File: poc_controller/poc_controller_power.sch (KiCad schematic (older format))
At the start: 8 parts

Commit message: Start assigning footprints and cleaning things up.
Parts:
- removed C? (x3): CP1, symbol CP1
- removed R?: R_Shunt, symbol R_Shunt
- added C13, C14, C15: 0.1uF, Capacitors_SMD:C_1206_HandSoldering, symbol C
- added R7: 0.001, Resistors_SMD:R_1206_HandSoldering, symbol R
- J6: renamed from J?; footprint (none) -> Connectors_Terminal_Blocks:TerminalBlock_bornier-2_P5.08mm; Part Number (none) -> ED1643-ND
- R8: renamed from R?; value R -> 15k; footprint (none) -> Resistors_SMD:R_1206_HandSoldering; Part Number (none) -> 311-15KERCT-ND
- R9: renamed from R?; value R -> 3.9k; footprint (none) -> Resistors_SMD:R_1206_HandSoldering; Part Number (none) -> 311-3.9KERCT-ND
- U6: renamed from U?; footprint (none) -> TO_SOT_Packages_SMD:TSOT-23-6; Part Number (none) -> 576-2749-1-ND
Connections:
- wire segments 20 -> 22
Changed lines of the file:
@@
 $Descr A4 11693 8268
 encoding utf-8
-Sheet 3 3
+Sheet 3 4
 Title ""
 Date ""
@@
 $EndDescr
 $Comp
-L CONN_01X02 J?
+L CONN_01X02 J6
 U 1 1 5A04E548
 P 3650 2250
-F 0 "J?" H 3650 2400 50  0000 C CNN
+F 0 "J6" H 3650 2400 50  0000 C CNN
 F 1 "CONN_01X02" V 3750 2250 50  0000 C CNN
-F 2 "" H 3650 2250 50  0001 C CNN
+F 2 "Connectors_Terminal_Blocks:TerminalBlock_bornier-2_P5.08mm" H 3650 2250 50  0001 C CNN
 F 3 "" H 3650 2250 50  0001 C CNN
+F 4 "ED1643-ND" H 3650 2250 60  0001 C CNN "Part Number"
 	1    3650 2250
 	1    0    0    -1
 $EndComp
 $Comp
-L R_Shunt R?
-U 1 1 5A04E5FB
-P 3050 2200
-F 0 "R?" V 2875 2200 50  0000 C CNN
-F 1 "R_Shunt" V 2950 2200 50  0000 C CNN
-F 2 "" V 2980 2200 50  0001 C CNN
-F 3 "" H 3050 2200 50  0001 C CNN
-	1    3050 2200
-	0    -1   -1   0
-$EndComp
-$Comp
-L VDD #PWR?
+L VDD #PWR31
 U 1 1 5A04E6EA
 P 2600 2100
-F 0 "#PWR?" H 2600 1950 50  0001 C CNN
+F 0 "#PWR31" H 2600 1950 50  0001 C CNN
 F 1 "VDD" H 2600 2250 50  0000 C CNN
 F 2 "" H 2600 2100 50  0001 C CNN
@@
 $EndComp
 $Comp
-L GND #PWR?
+L GND #PWR32
 U 1 1 5A04E708
 P 3300 2500
-F 0 "#PWR?" H 3300 2250 50  0001 C CNN
+F 0 "#PWR32" H 3300 2250 50  0001 C CNN
 F 1 "GND" H 3300 2350 50  0000 C CNN
 F 2 "" H 3300 2500 50  0001 C CNN
@@
 	1    0    0    -1
 $EndComp
-Text Label 3150 2050 1    60   ~ 0
+Text Label 3300 2050 1    60   ~ 0
 BATT_CURR_POS
-Text Label 2950 2050 1    60   ~ 0
+Text Label 2850 2050 1    60   ~ 0
 BATT_CURR_NEG
 $Comp
-L VDD #PWR?
+L VDD #PWR33
 U 1 1 5A04E87F
 P 5150 1450
-F 0 "#PWR?" H 5150 1300 50  0001 C CNN
+F 0 "#PWR33" H 5150 1300 50  0001 C CNN
 F 1 "VDD" H 5150 1600 50  0000 C CNN
 F 2 "" H 5150 1450 50  0001 C CNN
@@
 $EndComp
 $Comp
-L R R?
+L R R8
 U 1 1 5A04E899
 P 5150 1750
-F 0 "R?" V 5230 1750 50  0000 C CNN
-F 1 "R" V 5150 1750 50  0000 C CNN
-F 2 "" V 5080 1750 50  0001 C CNN
+F 0 "R8" V 5230 1750 50  0000 C CNN
+F 1 "15k" V 5150 1750 50  0000 C CNN
+F 2 "Resistors_SMD:R_1206_HandSoldering" V 5080 1750 50  0001 C CNN
 F 3 "" H 5150 1750 50  0001 C CNN
+F 4 "311-15KERCT-ND" V 5150 1750 60  0001 C CNN "Part Number"
 	1    5150 1750
 	1    0    0    -1
 $EndComp
 $Comp
-L R R?
+L R R9
 U 1 1 5A04E8C1
 P 5150 2250
-F 0 "R?" V 5230 2250 50  0000 C CNN
-F 1 "R" V 5150 2250 50  0000 C CNN
-F 2 "" V 5080 2250 50  0001 C CNN
+F 0 "R9" V 5230 2250 50  0000 C CNN
+F 1 "3.9k" V 5150 2250 50  0000 C CNN
+F 2 "Resistors_SMD:R_1206_HandSoldering" V 5080 2250 50  0001 C CNN
 F 3 "" H 5150 2250 50  0001 C CNN
+F 4 "311-3.9KERCT-ND" V 5150 2250 60  0001 C CNN "Part Number"
 	1    5150 2250
 	1    0    0    -1
 $EndComp
 $Comp
-L GND #PWR?
+L GND #PWR34
 U 1 1 5A04E8E3
 P 5150 2600
-F 0 "#PWR?" H 5150 2350 50  0001 C CNN
+F 0 "#PWR34" H 5150 2350 50  0001 C CNN
 F 1 "GND" H 5150 2450 50  0000 C CNN
 F 2 "" H 5150 2600 50  0001 C CNN
@@
 BATT_VOLT
 $Comp
-L MIC5211 U?
+L MIC5211 U6
 U 1 1 5A04EB3F
 P 7100 1850
-F 0 "U?" H 7450 1850 60  0000 C CNN
+F 0 "U6" H 7450 1850 60  0000 C CNN
 F 1 "MIC5211" H 7100 1850 60  0000 C CNN
-F 2 "" H 7100 1850 60  0001 C CNN
+F 2 "TO_SOT_Packages_SMD:TSOT-23-6" H 7100 1850 60  0001 C CNN
 F 3 "" H 7100 1850 60  0001 C CNN
+F 4 "576-2749-1-ND" H 7100 1850 60  0001 C CNN "Part Number"
 	1    7100 1850
 	1    0    0    -1
 $EndComp
 $Comp
-L GND #PWR?
+L GND #PWR36
 U 1 1 5A04EB7D
 P 6450 2350
-F 0 "#PWR?" H 6450 2100 50  0001 C CNN
+F 0 "#PWR36" H 6450 2100 50  0001 C CNN
 F 1 "GND" H 6450 2200 50  0000 C CNN
 F 2 "" H 6450 2350 50  0001 C CNN
@@
 $EndComp
 $Comp
-L VDD #PWR?
+L VDD #PWR35
 U 1 1 5A04EBA0
 P 6150 1800
-F 0 "#PWR?" H 6150 1650 50  0001 C CNN
+F 0 "#PWR35" H 6150 1650 50  0001 C CNN
 F 1 "VDD" H 6150 1950 50  0000 C CNN
 F 2 "" H 6150 1800 50  0001 C CNN
@@
 $EndComp
 $Comp
-L CP1 C?
-U 1 1 5A04EC9E
-P 7800 2500
-F 0 "C?" H 7825 2600 50  0000 L CNN
-F 1 "CP1" H 7825 2400 50  0000 L CNN
-F 2 "" H 7800 2500 50  0001 C CNN
-F 3 "" H 7800 2500 50  0001 C CNN
-	1    7800 2500
-	1    0    0    -1
-$EndComp
-$Comp
-L CP1 C?
-U 1 1 5A04ECDC
-P 8200 2350
-F 0 "C?" H 8225 2450 50  0000 L CNN
-F 1 "CP1" H 8225 2250 50  0000 L CNN
-F 2 "" H 8200 2350 50  0001 C CNN
-F 3 "" H 8200 2350 50  0001 C CNN
-	1    8200 2350
-	1    0    0    -1
-$EndComp
-$Comp
-L CP1 C?
-U 1 1 5A04ED0F
-P 8650 2150
-F 0 "C?" H 8675 2250 50  0000 L CNN
-F 1 "CP1" H 8675 2050 50  0000 L CNN
-F 2 "" H 8650 2150 50  0001 C CNN
-F 3 "" H 8650 2150 50  0001 C CNN
-	1    8650 2150
-	1    0    0    -1
-$EndComp
-$Comp
-L VDD #PWR?
+L VDD #PWR37
 U 1 1 5A04ED40
 P 7800 1750
-F 0 "#PWR?" H 7800 1600 50  0001 C CNN
+F 0 "#PWR37" H 7800 1600 50  0001 C CNN
 F 1 "VDD" H 7800 1900 50  0000 C CNN
 F 2 "" H 7800 1750 50  0001 C CNN
@@
 $EndComp
 $Comp
-L +3.3V #PWR?
+L +3.3V #PWR40
 U 1 1 5A04ED6C
 P 8400 2200
-F 0 "#PWR?" H 8400 2050 50  0001 C CNN
+F 0 "#PWR40" H 8400 2050 50  0001 C CNN
 F 1 "+3.3V" H 8400 2340 50  0000 C CNN
 F 2 "" H 8400 2200 50  0001 C CNN
@@
 $EndComp
 $Comp
-L +5V #PWR?
+L +5V #PWR42
 U 1 1 5A04ED98
 P 8850 2000
-F 0 "#PWR?" H 8850 1850 50  0001 C CNN
+F 0 "#PWR42" H 8850 1850 50  0001 C CNN
 F 1 "+5V" H 8850 2140 50  0000 C CNN
 F 2 "" H 8850 2000 50  0001 C CNN
@@
 $EndComp
 $Comp
-L GND #PWR?
+L GND #PWR39
 U 1 1 5A04EED4
 P 8200 2500
-F 0 "#PWR?" H 8200 2250 50  0001 C CNN
+F 0 "#PWR39" H 8200 2250 50  0001 C CNN
 F 1 "GND" H 8200 2350 50  0000 C CNN
 F 2 "" H 8200 2500 50  0001 C CNN
@@
 $EndComp
 $Comp
-L GND #PWR?
+L GND #PWR41
 U 1 1 5A04F080
 P 8650 2300
-F 0 "#PWR?" H 8650 2050 50  0001 C CNN
+F 0 "#PWR41" H 8650 2050 50  0001 C CNN
 F 1 "GND" H 8650 2150 50  0000 C CNN
 F 2 "" H 8650 2300 50  0001 C CNN
@@
 $EndComp
 $Comp
-L GND #PWR?
+L GND #PWR38
 U 1 1 5A04F187
 P 7800 2650
-F 0 "#PWR?" H 7800 2400 50  0001 C CNN
+F 0 "#PWR38" H 7800 2400 50  0001 C CNN
 F 1 "GND" H 7800 2500 50  0000 C CNN
 F 2 "" H 7800 2650 50  0001 C CNN
@@
 Text Label 1750 1100 0    60   ~ 0
 BATT_VOLT
+$Comp
+L C C14
+U 1 1 5AB69088
+P 8200 2350
+F 0 "C14" H 8225 2450 50  0000 L CNN
+F 1 "0.1uF" H 8225 2250 50  0000 L CNN
+F 2 "Capacitors_SMD:C_1206_HandSoldering" H 8238 2200 50  0001 C CNN
+F 3 "" H 8200 2350 50  0001 C CNN
+F 4 "311-1179-1-ND" H 8200 2350 60  0001 C CNN "Part Number"
+	1    8200 2350
+	1    0    0    -1
+$EndComp
+$Comp
+L C C15
+U 1 1 5AB690D6
+P 8650 2150
+F 0 "C15" H 8675 2250 50  0000 L CNN
+F 1 "0.1uF" H 8675 2050 50  0000 L CNN
+F 2 "Capacitors_SMD:C_1206_HandSoldering" H 8688 2000 50  0001 C CNN
+F 3 "" H 8650 2150 50  0001 C CNN
+F 4 "311-1179-1-ND" H 8650 2150 60  0001 C CNN "Part Number"
+	1    8650 2150
+	1    0    0    -1
+$EndComp
+$Comp
+L C C13
+U 1 1 5AB69385
+P 7800 2500
+F 0 "C13" H 7825 2600 50  0000 L CNN
+F 1 "0.1uF" H 7825 2400 50  0000 L CNN
+F 2 "Capacitors_SMD:C_1206_HandSoldering" H 7838 2350 50  0001 C CNN
+F 3 "" H 7800 2500 50  0001 C CNN
+F 4 "311-1179-1-ND" H 7800 2500 60  0001 C CNN "Part Number"
+	1    7800 2500
+	1    0    0    -1
+$EndComp
+$Comp
+L R R7
+U 1 1 5AB6A5BE
+P 3050 2200
+F 0 "R7" V 3130 2200 50  0000 C CNN
+F 1 "0.001" V 3050 2200 50  0000 C CNN
+F 2 "Resistors_SMD:R_1206_HandSoldering" V 2980 2200 50  0001 C CNN
+F 3 "" H 3050 2200 50  0001 C CNN
+F 4 "CSNL1206FT1L00CT-ND" V 3050 2200 60  0001 C CNN "Part Number"
+	1    3050 2200
+	0    1    1    0
+$EndComp
 Wire Wire Line
 	3450 2300 3300 2300
 Wire Wire Line
 	3300 2300 3300 2500
-Wire Wire Line
-	3250 2200 3450 2200
-Wire Wire Line
-	2850 2200 2600 2200
 Wire Wire Line
 	2600 2200 2600 2100
@@
 Wire Wire Line
 	1500 1100 1750 1100
+Wire Wire Line
+	3450 2200 3200 2200
+Wire Wire Line
+	2600 2200 2900 2200
+Connection ~ 3300 2200
+Wire Wire Line
+	3300 2200 3300 2050
+Connection ~ 2850 2200
+Wire Wire Line
+	2850 2050 2850 2200
 $EndSCHEMATC

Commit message: More design and component selection.
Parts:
- renumbered U6 to U4
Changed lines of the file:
@@
 LIBS:valves
 LIBS:quadcopter_lib
+LIBS:switches
 LIBS:poc_controller-cache
 EELAYER 25 0
@@
 $EndComp
 $Comp
-L VDD #PWR31
+L VDD #PWR27
 U 1 1 5A04E6EA
 P 2600 2100
-F 0 "#PWR31" H 2600 1950 50  0001 C CNN
+F 0 "#PWR27" H 2600 1950 50  0001 C CNN
 F 1 "VDD" H 2600 2250 50  0000 C CNN
 F 2 "" H 2600 2100 50  0001 C CNN
@@
 $EndComp
 $Comp
-L GND #PWR32
+L GND #PWR28
 U 1 1 5A04E708
 P 3300 2500
-F 0 "#PWR32" H 3300 2250 50  0001 C CNN
+F 0 "#PWR28" H 3300 2250 50  0001 C CNN
 F 1 "GND" H 3300 2350 50  0000 C CNN
 F 2 "" H 3300 2500 50  0001 C CNN
@@
 BATT_CURR_NEG
 $Comp
-L VDD #PWR33
+L VDD #PWR29
 U 1 1 5A04E87F
 P 5150 1450
-F 0 "#PWR33" H 5150 1300 50  0001 C CNN
+F 0 "#PWR29" H 5150 1300 50  0001 C CNN
 F 1 "VDD" H 5150 1600 50  0000 C CNN
 F 2 "" H 5150 1450 50  0001 C CNN
@@
 $EndComp
 $Comp
-L GND #PWR34
+L GND #PWR30
 U 1 1 5A04E8E3
 P 5150 2600
-F 0 "#PWR34" H 5150 2350 50  0001 C CNN
+F 0 "#PWR30" H 5150 2350 50  0001 C CNN
 F 1 "GND" H 5150 2450 50  0000 C CNN
 F 2 "" H 5150 2600 50  0001 C CNN
@@
 BATT_VOLT
 $Comp
-L MIC5211 U6
+L MIC5211 U4
 U 1 1 5A04EB3F
 P 7100 1850
-F 0 "U6" H 7450 1850 60  0000 C CNN
+F 0 "U4" H 7450 1850 60  0000 C CNN
 F 1 "MIC5211" H 7100 1850 60  0000 C CNN
 F 2 "TO_SOT_Packages_SMD:TSOT-23-6" H 7100 1850 60  0001 C CNN
@@
 $EndComp
 $Comp
-L GND #PWR36
+L GND #PWR32
 U 1 1 5A04EB7D
 P 6450 2350
-F 0 "#PWR36" H 6450 2100 50  0001 C CNN
+F 0 "#PWR32" H 6450 2100 50  0001 C CNN
 F 1 "GND" H 6450 2200 50  0000 C CNN
 F 2 "" H 6450 2350 50  0001 C CNN
@@
 $EndComp
 $Comp
-L VDD #PWR35
+L VDD #PWR31
 U 1 1 5A04EBA0
 P 6150 1800
-F 0 "#PWR35" H 6150 1650 50  0001 C CNN
+F 0 "#PWR31" H 6150 1650 50  0001 C CNN
 F 1 "VDD" H 6150 1950 50  0000 C CNN
 F 2 "" H 6150 1800 50  0001 C CNN
@@
 $EndComp
 $Comp
-L VDD #PWR37
+L VDD #PWR33
 U 1 1 5A04ED40
 P 7800 1750
-F 0 "#PWR37" H 7800 1600 50  0001 C CNN
+F 0 "#PWR33" H 7800 1600 50  0001 C CNN
 F 1 "VDD" H 7800 1900 50  0000 C CNN
 F 2 "" H 7800 1750 50  0001 C CNN
@@
 $EndComp
 $Comp
-L +3.3V #PWR40
+L +3.3V #PWR36
 U 1 1 5A04ED6C
 P 8400 2200
-F 0 "#PWR40" H 8400 2050 50  0001 C CNN
+F 0 "#PWR36" H 8400 2050 50  0001 C CNN
 F 1 "+3.3V" H 8400 2340 50  0000 C CNN
 F 2 "" H 8400 2200 50  0001 C CNN
@@
 $EndComp
 $Comp
-L +5V #PWR42
+L +5V #PWR38
 U 1 1 5A04ED98
 P 8850 2000
-F 0 "#PWR42" H 8850 1850 50  0001 C CNN
+F 0 "#PWR38" H 8850 1850 50  0001 C CNN
 F 1 "+5V" H 8850 2140 50  0000 C CNN
 F 2 "" H 8850 2000 50  0001 C CNN
@@
 $EndComp
 $Comp
-L GND #PWR39
+L GND #PWR35
 U 1 1 5A04EED4
 P 8200 2500
-F 0 "#PWR39" H 8200 2250 50  0001 C CNN
+F 0 "#PWR35" H 8200 2250 50  0001 C CNN
 F 1 "GND" H 8200 2350 50  0000 C CNN
 F 2 "" H 8200 2500 50  0001 C CNN
@@
 $EndComp
 $Comp
-L GND #PWR41
+L GND #PWR37
 U 1 1 5A04F080
 P 8650 2300
-F 0 "#PWR41" H 8650 2050 50  0001 C CNN
+F 0 "#PWR37" H 8650 2050 50  0001 C CNN
 F 1 "GND" H 8650 2150 50  0000 C CNN
 F 2 "" H 8650 2300 50  0001 C CNN
@@
 $EndComp
 $Comp
-L GND #PWR38
+L GND #PWR34
 U 1 1 5A04F187
 P 7800 2650
-F 0 "#PWR38" H 7800 2400 50  0001 C CNN
+F 0 "#PWR34" H 7800 2400 50  0001 C CNN
 F 1 "GND" H 7800 2500 50  0000 C CNN
 F 2 "" H 7800 2650 50  0001 C CNN

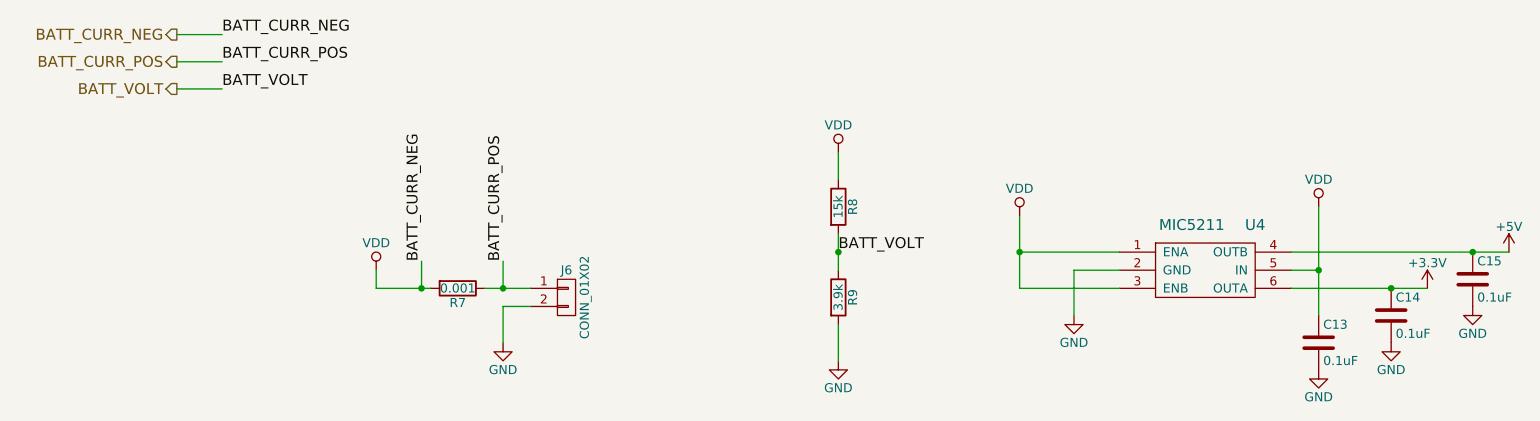
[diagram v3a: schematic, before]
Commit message: Add UART level shifting.
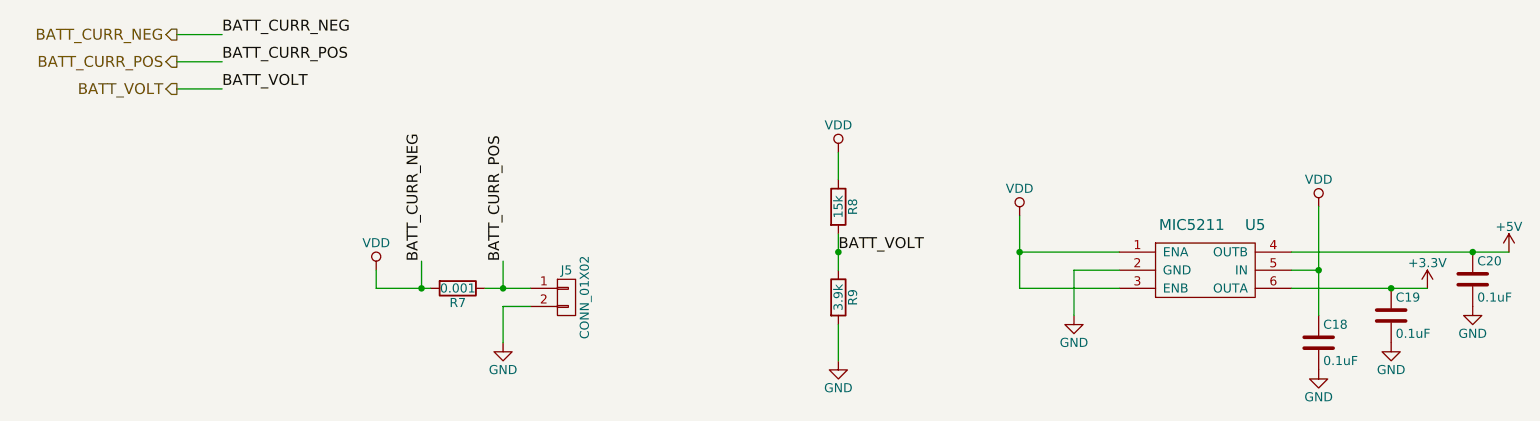
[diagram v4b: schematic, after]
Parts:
- renumbered C13 to C18, C14 to C19, C15 to C20, J6 to J5, U4 to U5
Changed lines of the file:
@@
 $EndDescr
 $Comp
-L CONN_01X02 J6
+L CONN_01X02 J5
 U 1 1 5A04E548
 P 3650 2250
-F 0 "J6" H 3650 2400 50  0000 C CNN
+F 0 "J5" H 3650 2400 50  0000 C CNN
 F 1 "CONN_01X02" V 3750 2250 50  0000 C CNN
 F 2 "Connectors_Terminal_Blocks:TerminalBlock_bornier-2_P5.08mm" H 3650 2250 50  0001 C CNN
@@
 $EndComp
 $Comp
-L VDD #PWR027
+L VDD #PWR32
 U 1 1 5A04E6EA
 P 2600 2100
-F 0 "#PWR027" H 2600 1950 50  0001 C CNN
+F 0 "#PWR32" H 2600 1950 50  0001 C CNN
 F 1 "VDD" H 2600 2250 50  0000 C CNN
 F 2 "" H 2600 2100 50  0001 C CNN
@@
 $EndComp
 $Comp
-L GND #PWR028
+L GND #PWR33
 U 1 1 5A04E708
 P 3300 2500
-F 0 "#PWR028" H 3300 2250 50  0001 C CNN
+F 0 "#PWR33" H 3300 2250 50  0001 C CNN
 F 1 "GND" H 3300 2350 50  0000 C CNN
 F 2 "" H 3300 2500 50  0001 C CNN
@@
 BATT_CURR_NEG
 $Comp
-L VDD #PWR029
+L VDD #PWR34
 U 1 1 5A04E87F
 P 5150 1450
-F 0 "#PWR029" H 5150 1300 50  0001 C CNN
+F 0 "#PWR34" H 5150 1300 50  0001 C CNN
 F 1 "VDD" H 5150 1600 50  0000 C CNN
 F 2 "" H 5150 1450 50  0001 C CNN
@@
 $EndComp
 $Comp
-L GND #PWR030
+L GND #PWR35
 U 1 1 5A04E8E3
 P 5150 2600
-F 0 "#PWR030" H 5150 2350 50  0001 C CNN
+F 0 "#PWR35" H 5150 2350 50  0001 C CNN
 F 1 "GND" H 5150 2450 50  0000 C CNN
 F 2 "" H 5150 2600 50  0001 C CNN
@@
 BATT_VOLT
 $Comp
-L MIC5211 U4
+L MIC5211 U5
 U 1 1 5A04EB3F
 P 7100 1850
-F 0 "U4" H 7450 1850 60  0000 C CNN
+F 0 "U5" H 7450 1850 60  0000 C CNN
 F 1 "MIC5211" H 7100 1850 60  0000 C CNN
 F 2 "TO_SOT_Packages_SMD:TSOT-23-6" H 7100 1850 60  0001 C CNN
@@
 $EndComp
 $Comp
-L GND #PWR031
+L GND #PWR37
 U 1 1 5A04EB7D
 P 6450 2350
-F 0 "#PWR031" H 6450 2100 50  0001 C CNN
+F 0 "#PWR37" H 6450 2100 50  0001 C CNN
 F 1 "GND" H 6450 2200 50  0000 C CNN
 F 2 "" H 6450 2350 50  0001 C CNN
@@
 $EndComp
 $Comp
-L VDD #PWR032
+L VDD #PWR36
 U 1 1 5A04EBA0
 P 6150 1800
-F 0 "#PWR032" H 6150 1650 50  0001 C CNN
+F 0 "#PWR36" H 6150 1650 50  0001 C CNN
 F 1 "VDD" H 6150 1950 50  0000 C CNN
 F 2 "" H 6150 1800 50  0001 C CNN
@@
 $EndComp
 $Comp
-L VDD #PWR033
+L VDD #PWR38
 U 1 1 5A04ED40
 P 7800 1750
-F 0 "#PWR033" H 7800 1600 50  0001 C CNN
+F 0 "#PWR38" H 7800 1600 50  0001 C CNN
 F 1 "VDD" H 7800 1900 50  0000 C CNN
 F 2 "" H 7800 1750 50  0001 C CNN
@@
 $EndComp
 $Comp
-L +3.3V #PWR034
+L +3.3V #PWR41
 U 1 1 5A04ED6C
 P 8400 2200
-F 0 "#PWR034" H 8400 2050 50  0001 C CNN
+F 0 "#PWR41" H 8400 2050 50  0001 C CNN
 F 1 "+3.3V" H 8400 2340 50  0000 C CNN
 F 2 "" H 8400 2200 50  0001 C CNN
@@
 $EndComp
 $Comp
-L +5V #PWR035
+L +5V #PWR43
 U 1 1 5A04ED98
 P 8850 2000
-F 0 "#PWR035" H 8850 1850 50  0001 C CNN
+F 0 "#PWR43" H 8850 1850 50  0001 C CNN
 F 1 "+5V" H 8850 2140 50  0000 C CNN
 F 2 "" H 8850 2000 50  0001 C CNN
@@
 $EndComp
 $Comp
-L GND #PWR036
+L GND #PWR40
 U 1 1 5A04EED4
 P 8200 2500
-F 0 "#PWR036" H 8200 2250 50  0001 C CNN
+F 0 "#PWR40" H 8200 2250 50  0001 C CNN
 F 1 "GND" H 8200 2350 50  0000 C CNN
 F 2 "" H 8200 2500 50  0001 C CNN
@@
 $EndComp
 $Comp
-L GND #PWR037
+L GND #PWR42
 U 1 1 5A04F080
 P 8650 2300
-F 0 "#PWR037" H 8650 2050 50  0001 C CNN
+F 0 "#PWR42" H 8650 2050 50  0001 C CNN
 F 1 "GND" H 8650 2150 50  0000 C CNN
 F 2 "" H 8650 2300 50  0001 C CNN
@@
 $EndComp
 $Comp
-L GND #PWR038
+L GND #PWR39
 U 1 1 5A04F187
 P 7800 2650
-F 0 "#PWR038" H 7800 2400 50  0001 C CNN
+F 0 "#PWR39" H 7800 2400 50  0001 C CNN
 F 1 "GND" H 7800 2500 50  0000 C CNN
 F 2 "" H 7800 2650 50  0001 C CNN
@@
 BATT_VOLT
 $Comp
-L C C14
+L C C19
 U 1 1 5AB69088
 P 8200 2350
-F 0 "C14" H 8225 2450 50  0000 L CNN
+F 0 "C19" H 8225 2450 50  0000 L CNN
 F 1 "0.1uF" H 8225 2250 50  0000 L CNN
 F 2 "Capacitors_SMD:C_1206_HandSoldering" H 8238 2200 50  0001 C CNN
@@
 $EndComp
 $Comp
-L C C15
+L C C20
 U 1 1 5AB690D6
 P 8650 2150
-F 0 "C15" H 8675 2250 50  0000 L CNN
+F 0 "C20" H 8675 2250 50  0000 L CNN
 F 1 "0.1uF" H 8675 2050 50  0000 L CNN
 F 2 "Capacitors_SMD:C_1206_HandSoldering" H 8688 2000 50  0001 C CNN
@@
 $EndComp
 $Comp
-L C C13
+L C C18
 U 1 1 5AB69385
 P 7800 2500
-F 0 "C13" H 7825 2600 50  0000 L CNN
+F 0 "C18" H 7825 2600 50  0000 L CNN
 F 1 "0.1uF" H 7825 2400 50  0000 L CNN
 F 2 "Capacitors_SMD:C_1206_HandSoldering" H 7838 2350 50  0001 C CNN
